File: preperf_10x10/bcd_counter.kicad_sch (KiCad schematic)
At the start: 16 parts, among them U11 74LS73, U12 74LS73, U13 74LS08, U14 74LS32, U8 4511, U9 D168K

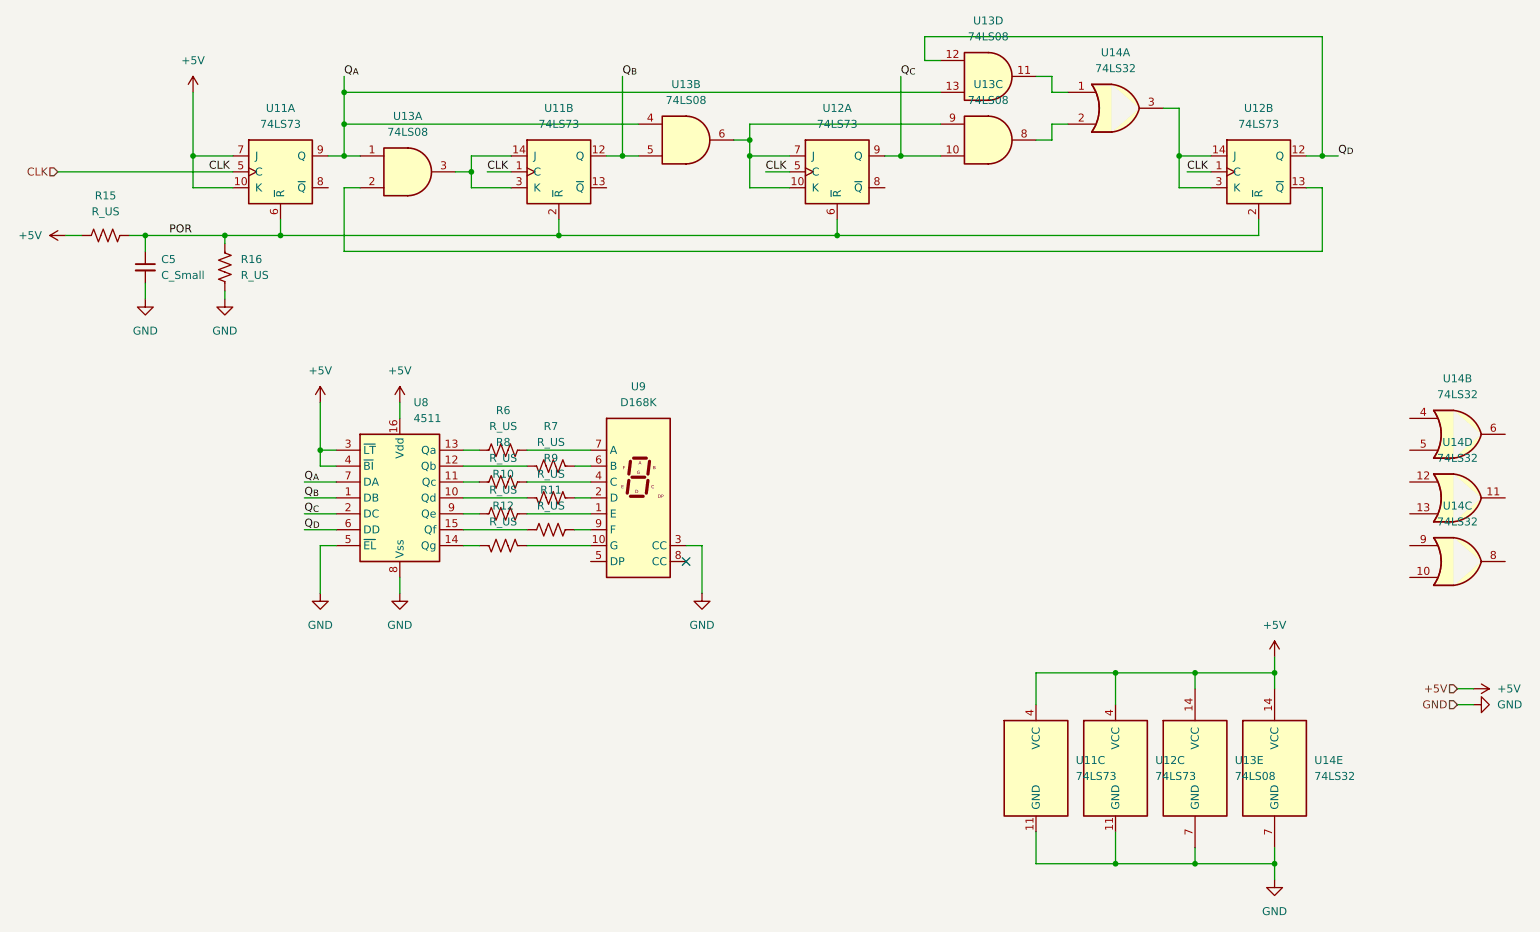
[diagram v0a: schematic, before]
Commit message: Fix BCD UP counter
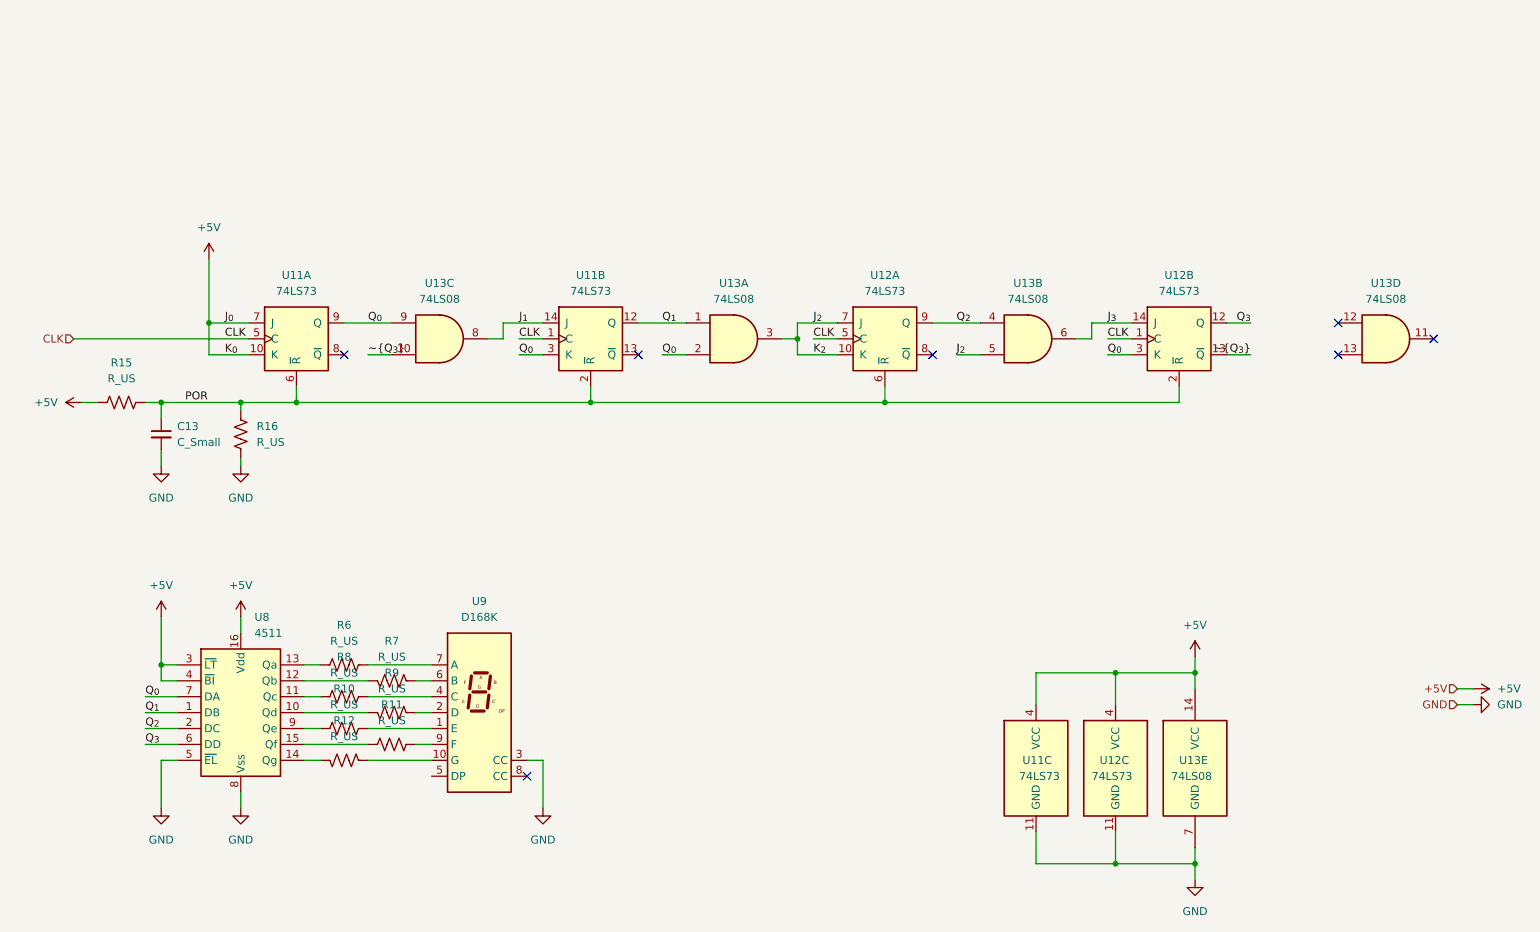
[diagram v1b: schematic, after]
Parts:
- removed U14: 74LS32, Package_DIP:DIP-14_W7.62mm_Socket, symbol 74xx:74LS32
- renumbered C5 to C13
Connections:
- net Q_{0}: now reaches U13.2
- net Q_{0}: now also U11.3 (K), U11.9 (Q), U12.3 (K), U13.9, U8.7 (DA); no longer U12.13 (~{Q})
- net J_{1}: now reaches U13.8
- net J_{1}: now also U11.14 (J)
- net J_{2}: now reaches U12.10 (K), U12.7 (J)
- net J_{2}: now also U13.3, U13.5; no longer U13.6, U13.9
- net J_{3}: now reaches U12.14 (J)
- net J_{3}: now also U13.6; no longer U12.3 (K)
- removed net Q_{A}: U11.9 (Q), U13.1, U13.13, U13.4, U8.7 (DA)
- net Q_{B} renamed Q_{1}
- net Q_{1}: now also U13.1; no longer U13.5
- net Q_{C} renamed Q_{2}
- net Q_{2}: now also U13.4; no longer U13.10
- net Q_{D} renamed Q_{3}
- net Q_{3}: no longer U13.12
- new net ~{Q_{3}}: U12.13 (~{Q}), U13.10
- no-connect marks 1 -> 7
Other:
- moved on the sheet: C13, R10, R11, R12, R15, R16, R6, R7, R8, R9, U11A, U11B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

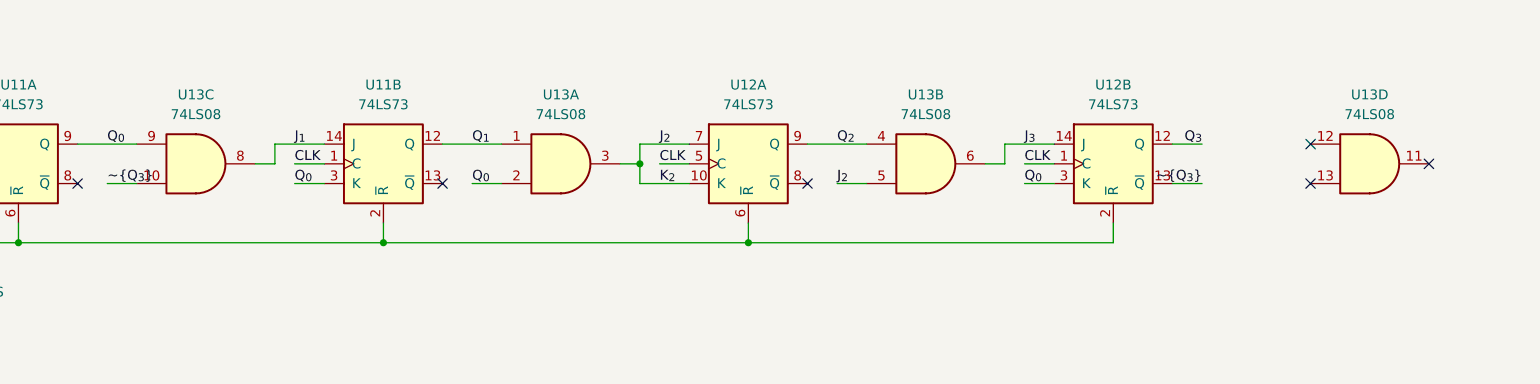
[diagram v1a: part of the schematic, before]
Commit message: [ADD] Digital Logic Design project (FIUBA): PCB implementation of schmitt triggers, logic functions, counters, state machines, and logic probes
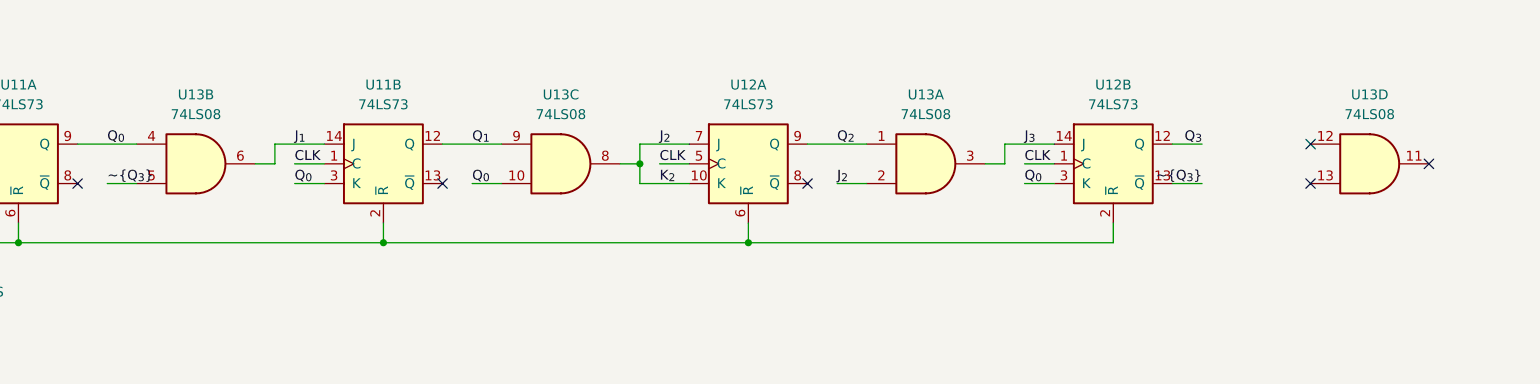
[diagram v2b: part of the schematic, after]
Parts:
- R15: footprint Resistor_THT:R_Axial_DIN0207_L6.3mm_D2.5mm_P7.62mm_Horizontal -> Resistor_THT:R_Axial_DIN0207_L6.3mm_D2.5mm_P2.54mm_Vertical
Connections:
- net J_{1}: now also U13.6; no longer U13.8
- net J_{2}: now also U13.2, U13.8; no longer U13.3, U13.5
- net J_{3}: now also U13.3; no longer U13.6
- net Q_{0}: now also U13.10, U13.4; no longer U13.2, U13.9
- net Q_{1}: now also U13.9; no longer U13.1
- net Q_{2}: now also U13.1; no longer U13.4
- net ~{Q_{3}}: now also U13.5; no longer U13.10
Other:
- moved on the sheet: U13A, U13B, U13C
